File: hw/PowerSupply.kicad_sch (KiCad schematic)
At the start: 17 parts, among them U1200 TLV62150A, U1201 TPS22976, U1202 TPS22976

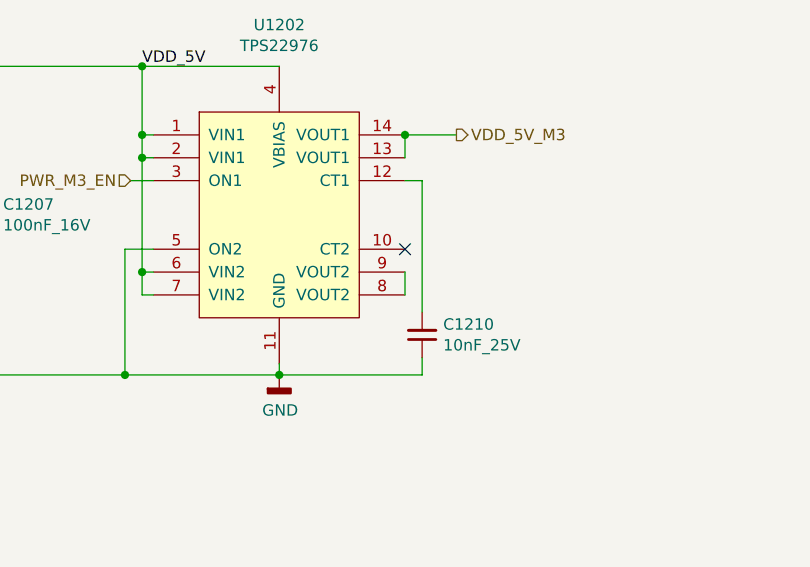
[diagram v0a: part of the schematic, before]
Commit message: Update schematic:
- Add ESD protection.
- Adjust distance bolts so they fit to the MX mounting plate.
- Make key layout symmetric.
- Add resistor to TX driver outputs.
- Use alternate IO functions on inter-board connectors.
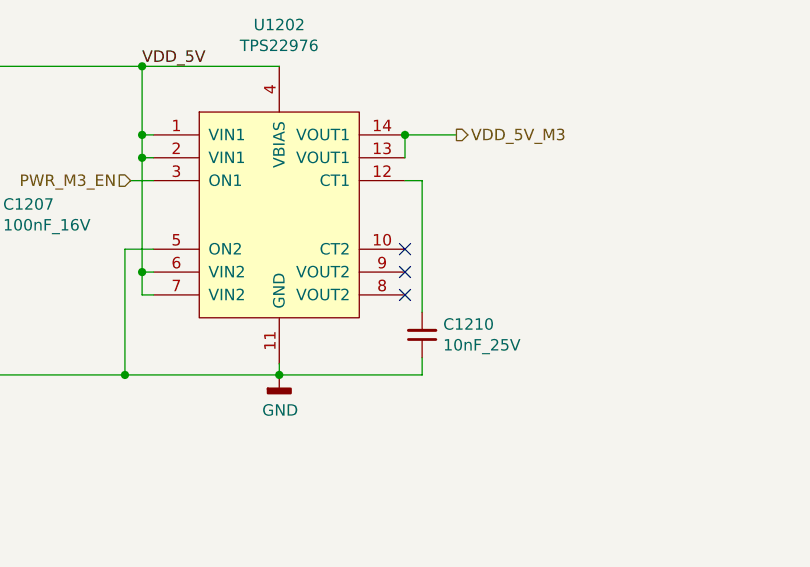
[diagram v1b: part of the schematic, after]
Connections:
- net at U1202.8 (VOUT2): no longer U1202.9 (VOUT2)
- no-connect marks 1 -> 3
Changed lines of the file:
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@@
   )
   (no_connect (at 167.64 115.57))
+  (no_connect (at 167.64 118.11))
+  (no_connect (at 167.64 120.65))
   (wire (pts (xy 78.74 107.95) (xy 98.425 107.95))
     (stroke (width 0) (type default) (color 0 0 0 0))
@@
     (stroke (width 0) (type default) (color 0 0 0 0))
   )
-  (wire (pts (xy 167.64 120.65) (xy 167.64 118.11))
-    (stroke (width 0) (type default) (color 0 0 0 0))
-  )

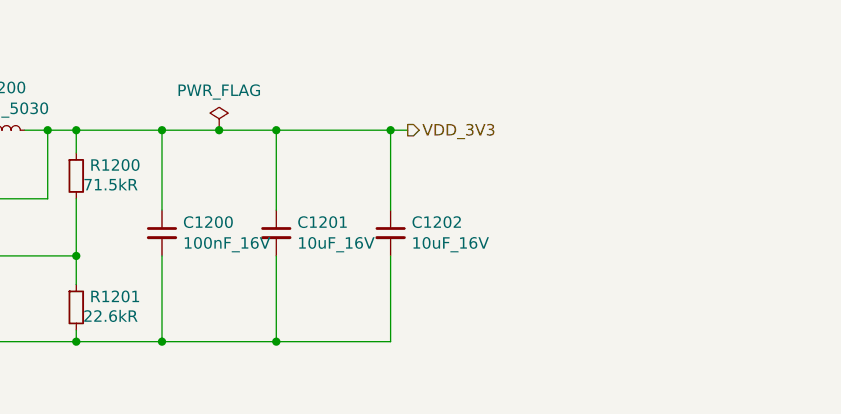
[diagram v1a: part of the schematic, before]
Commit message: Add current probes to 3.3V and pull-up to LV_EN.
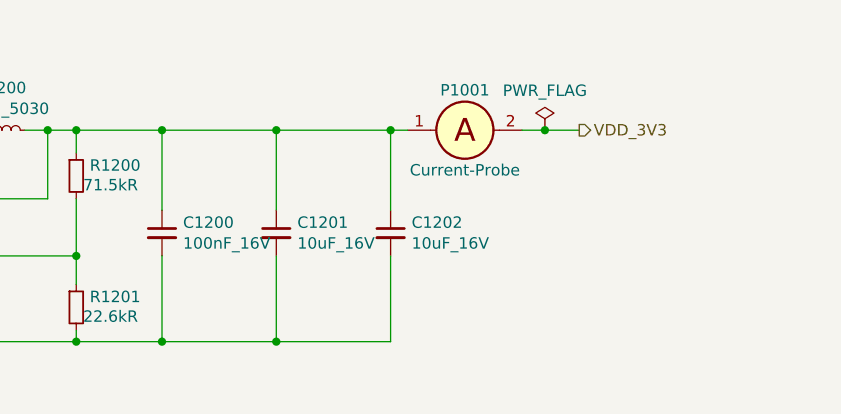
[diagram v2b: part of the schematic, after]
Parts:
- added P1001: Current-Probe, Keyboard:Current-Probe-2.54, symbol Keyboard:Current-Probe
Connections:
- net VDD_3V3: now also P1001.2; no longer C1200.1, C1201.1, C1202.1, L1200.2, R1200.1, U1200.14 (VOS), U1200.7 (FSW)
- new net: C1200.1, C1201.1, C1202.1, L1200.2, P1001.1, R1200.1, U1200.14 (VOS), U1200.7 (FSW)
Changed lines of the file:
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@@
   (junction (at 49.53 105.41) (diameter 0) (color 0 0 0 0)
   )
+  (junction (at 102.235 52.07) (diameter 0) (color 0 0 0 0)
+  )
+  (junction (at 137.795 44.45) (diameter 0) (color 0 0 0 0)
+  )
+  (junction (at 125.095 44.45) (diameter 0) (color 0 0 0 0)
+  )
+  (junction (at 80.645 129.54) (diameter 0) (color 0 0 0 0)
+  )
+  (junction (at 153.67 129.54) (diameter 0) (color 0 0 0 0)
+  )
+  (junction (at 42.545 44.45) (diameter 0) (color 0 0 0 0)
+  )
+  (junction (at 102.235 46.99) (diameter 0) (color 0 0 0 0)
+  )
+  (junction (at 112.395 44.45) (diameter 0) (color 0 0 0 0)
+  )
+  (junction (at 49.53 118.11) (diameter 0) (color 0 0 0 0)
+  )
+  (junction (at 71.755 46.99) (diameter 0) (color 0 0 0 0)
+  )
+  (junction (at 90.805 67.945) (diameter 0) (color 0 0 0 0)
+  )
+  (junction (at 49.53 95.25) (diameter 0) (color 0 0 0 0)
+  )
   (junction (at 150.495 44.45) (diameter 0) (color 0 0 0 0)
   )
-  (junction (at 102.235 52.07) (diameter 0) (color 0 0 0 0)
-  )
-  (junction (at 137.795 44.45) (diameter 0) (color 0 0 0 0)
-  )
-  (junction (at 125.095 44.45) (diameter 0) (color 0 0 0 0)
-  )
-  (junction (at 80.645 129.54) (diameter 0) (color 0 0 0 0)
-  )
-  (junction (at 153.67 129.54) (diameter 0) (color 0 0 0 0)
-  )
-  (junction (at 42.545 44.45) (diameter 0) (color 0 0 0 0)
-  )
-  (junction (at 102.235 46.99) (diameter 0) (color 0 0 0 0)
-  )
-  (junction (at 112.395 44.45) (diameter 0) (color 0 0 0 0)
-  )
-  (junction (at 49.53 118.11) (diameter 0) (color 0 0 0 0)
-  )
-  (junction (at 71.755 46.99) (diameter 0) (color 0 0 0 0)
-  )
-  (junction (at 90.805 67.945) (diameter 0) (color 0 0 0 0)
-  )
-  (junction (at 49.53 95.25) (diameter 0) (color 0 0 0 0)
-  )
   (junction (at 138.43 102.87) (diameter 0) (color 0 0 0 0)
   )
@@
   (junction (at 78.74 118.11) (diameter 0) (color 0 0 0 0)
   )
-  (junction (at 131.445 44.45) (diameter 0) (color 0 0 0 0)
+  (junction (at 167.64 44.45) (diameter 0) (color 0 0 0 0)
   )
   (no_connect (at 167.64 115.57))
@@
     (stroke (width 0) (type default) (color 0 0 0 0))
   )
-  (wire (pts (xy 150.495 44.45) (xy 152.4 44.45))
-    (stroke (width 0) (type default) (color 0 0 0 0))
-  )
   (wire (pts (xy 138.43 95.25) (xy 138.43 102.87))
     (stroke (width 0) (type default) (color 0 0 0 0))
@@
     (stroke (width 0) (type default) (color 0 0 0 0))
   )
-  (wire (pts (xy 125.095 44.45) (xy 131.445 44.45))
-    (stroke (width 0) (type default) (color 0 0 0 0))
-  )
   (wire (pts (xy 50.8 118.11) (xy 49.53 118.11))
     (stroke (width 0) (type default) (color 0 0 0 0))
@@
     (stroke (width 0) (type default) (color 0 0 0 0))
   )
-  (wire (pts (xy 131.445 44.45) (xy 137.795 44.45))
+  (wire (pts (xy 125.095 44.45) (xy 137.795 44.45))
     (stroke (width 0) (type default) (color 0 0 0 0))
   )
@@
     (stroke (width 0) (type default) (color 0 0 0 0))
   )
+  (wire (pts (xy 165.1 44.45) (xy 167.64 44.45))
+    (stroke (width 0) (type default) (color 0 0 0 0))
+  )
   (wire (pts (xy 88.265 69.215) (xy 88.265 67.945))
     (stroke (width 0) (type default) (color 0 0 0 0))
@@
     (stroke (width 0) (type default) (color 0 0 0 0))
   )
+  (wire (pts (xy 167.64 44.45) (xy 171.45 44.45))
+    (stroke (width 0) (type default) (color 0 0 0 0))
+  )
   (wire (pts (xy 102.235 58.42) (xy 115.57 58.42))
     (stroke (width 0) (type default) (color 0 0 0 0))
@@
   )
   (wire (pts (xy 55.245 44.45) (xy 71.755 44.45))
+    (stroke (width 0) (type default) (color 0 0 0 0))
+  )
+  (wire (pts (xy 152.4 44.45) (xy 150.495 44.45))
     (stroke (width 0) (type default) (color 0 0 0 0))
   )
@@
     (effects (font (size 1.27 1.27)) (justify right))
   )
-  (hierarchical_label "VDD_3V3" (shape output) (at 152.4 44.45 0)
+  (hierarchical_label "VDD_3V3" (shape output) (at 171.45 44.45 0)
     (effects (font (size 1.27 1.27)) (justify left))
   )
@@
     (pin "2")
   )
-  (symbol (lib_id "Keyboard:PWR_FLAG") (at 131.445 44.45 0) (unit 1)
-    (in_bom yes) (on_board yes)
-    (property "Reference" "#FLG01200" (id 0) (at 131.445 42.545 0)
-      (effects (font (size 1.27 1.27)) hide)
-    )
-    (property "Value" "PWR_FLAG" (id 1) (at 131.445 40.0558 0))
-    (property "Footprint" "" (id 2) (at 131.445 44.45 0)
-      (effects (font (size 1.27 1.27)) hide)
-    )
-    (property "Datasheet" "~" (id 3) (at 131.445 44.45 0)
-      (effects (font (size 1.27 1.27)) hide)
-    )
-    (pin "1")
+  (symbol (lib_id "Keyboard:PWR_FLAG") (at 167.64 44.45 0) (unit 1)
+    (in_bom yes) (on_board yes)
+    (property "Reference" "#FLG01200" (id 0) (at 167.64 42.545 0)
+      (effects (font (size 1.27 1.27)) hide)
+    )
+    (property "Value" "PWR_FLAG" (id 1) (at 167.64 40.0558 0))
+    (property "Footprint" "" (id 2) (at 167.64 44.45 0)
+      (effects (font (size 1.27 1.27)) hide)
+    )
+    (property "Datasheet" "~" (id 3) (at 167.64 44.45 0)
+      (effects (font (size 1.27 1.27)) hide)
+    )
+    (pin "1")
+  )
+  (symbol (lib_id "Keyboard:Current-Probe") (at 158.75 44.45 0) (unit 1)
+    (in_bom yes) (on_board yes)
+    (property "Reference" "P1001" (id 0) (at 158.75 40.005 0))
+    (property "Value" "Current-Probe" (id 1) (at 158.75 48.895 0))
+    (property "Footprint" "Keyboard:Current-Probe-2.54" (id 2) (at 158.75 45.466 0)
+      (effects (font (size 1.27 1.27)) hide)
+    )
+    (property "Datasheet" "" (id 3) (at 158.75 45.466 0)
+      (effects (font (size 1.27 1.27)) hide)
+    )
+    (pin "1")
+    (pin "2")
   )
 )

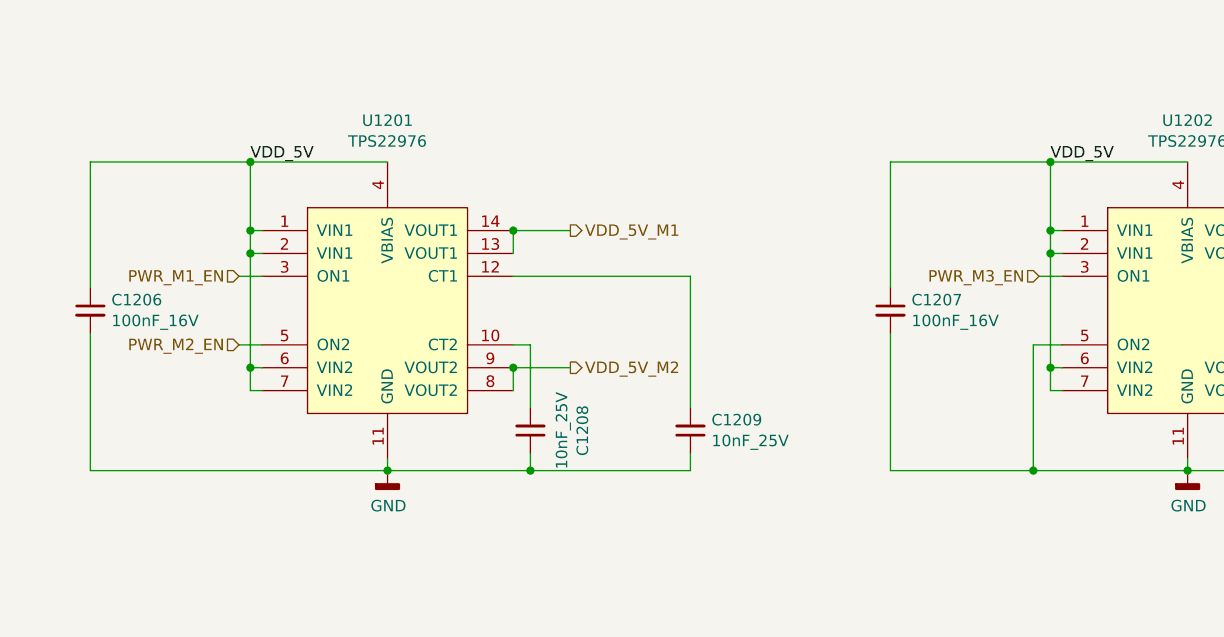
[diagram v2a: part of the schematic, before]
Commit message: Add pull-downs to power switches.
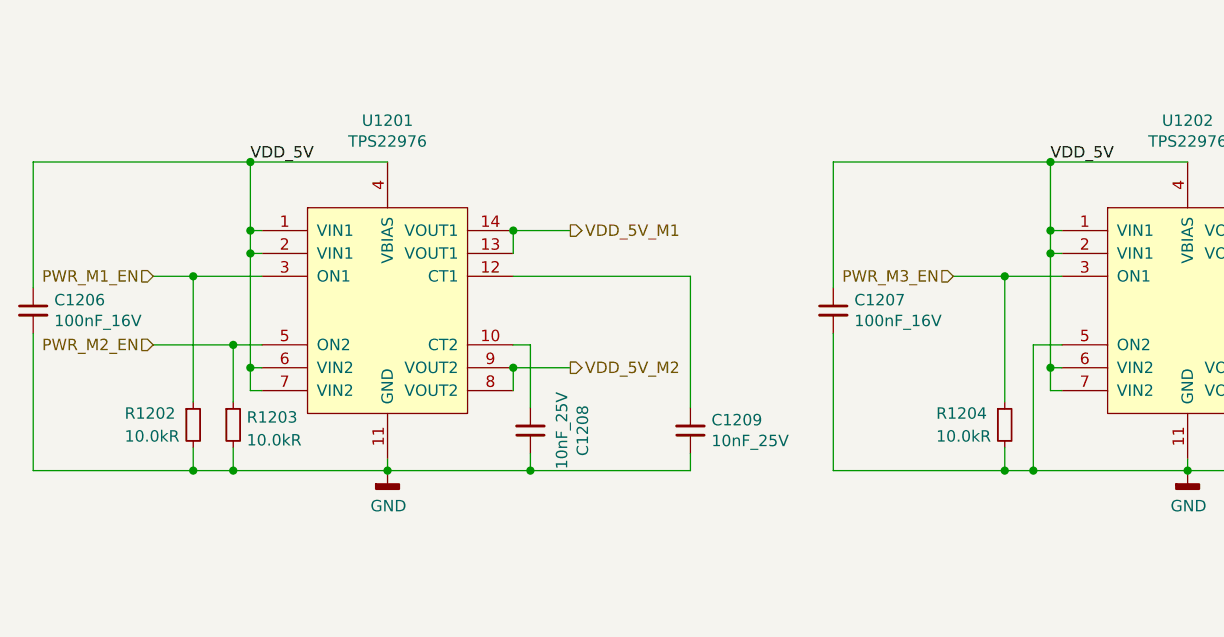
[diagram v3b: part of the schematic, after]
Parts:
- added R1202, R1203, R1204: 10.0kR, Keyboard:R_0402, symbol Keyboard:10.0kR
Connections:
- net GND: now also R1202.2, R1203.2, R1204.2
- net PWR_M1_EN: now also R1202.1
- net PWR_M2_EN: now also R1203.1
- net PWR_M3_EN: now also R1204.1
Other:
- moved on the sheet: C1206, C1207
